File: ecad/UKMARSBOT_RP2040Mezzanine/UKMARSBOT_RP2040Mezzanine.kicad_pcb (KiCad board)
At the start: 2 copper layers, 99.1 x 81.3 mm, 20 parts, among them J3 Conn_01x06, J4 Conn_01x06, J5 Conn_01x03, J6 POWER, J7 Switch, M1 CONN_06SILK_FEMALE_PTH, M1 Left MOTOR, M2  CONN_06SILK_FEMALE_PTH, M2 Right MOTOR, U2 LM7805_TO220

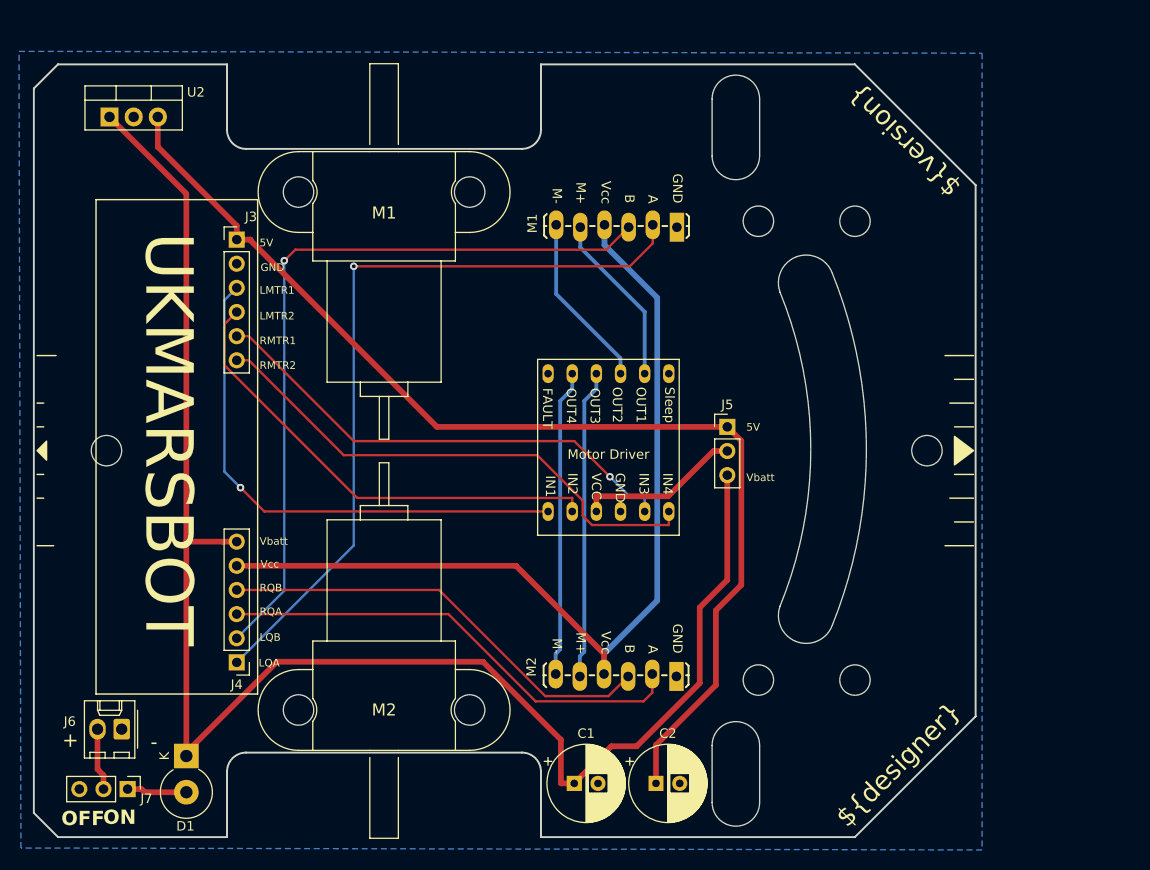
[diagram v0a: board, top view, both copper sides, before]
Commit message: fixed ignore file. Libraries from previous project. A verison of chassis, mezzanine and sensor board. Needed to play with connector locations. Nothing completly finished but i think the chassis and mezzanine are 90%
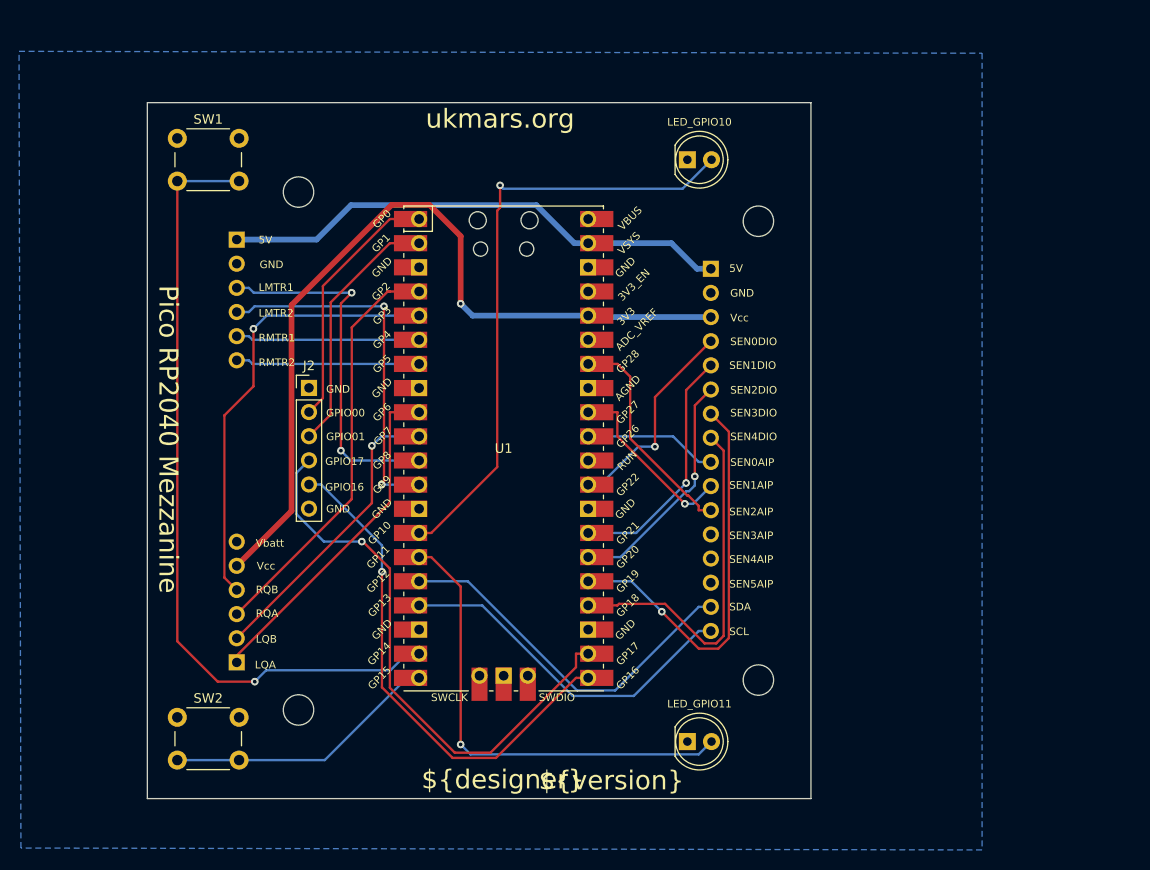
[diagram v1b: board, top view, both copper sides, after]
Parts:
- removed C1, C2: 330uF, 16V, Capacitor_THT:CP_Radial_D8.0mm_P2.50mm
- removed D1: 1N5401, Diode_THT:D_DO-201AE_P3.81mm_Vertical_KathodeUp
- removed H5, H6: MountingHole, ukmarsbot:MountingHole_3.2mm_M3_clearance
- removed J5: Conn_01x03, Connector_PinHeader_2.54mm:PinHeader_1x03_P2.54mm_Vertical
- removed J6: POWER, Connector_Molex:Molex_KK-254_AE-6410-02A_1x02_P2.54mm_Vertical
- removed J7: Switch, Connector_PinHeader_2.54mm:PinHeader_1x03_P2.54mm_Vertical
- removed M1: Left MOTOR, ukmarsbot:MINI-METAL-GEARMOTOR-WITH-BRACKET_Alt
- removed M1: CONN_06SILK_FEMALE_PTH, ukmarsbot:1X06_LOCK_LONGPADS
- removed M2: Right MOTOR, ukmarsbot:MINI-METAL-GEARMOTOR-WITH-BRACKET
- removed M2 : CONN_06SILK_FEMALE_PTH, ukmarsbot:1X06_LOCK_LONGPADS
- removed Motor Driver: DVR8833_DC_Controller, PBFootPrintLibrary:DRV8833_DC_Controller
- removed U2: LM7805_TO220, Package_TO_SOT_THT:TO-220-3_Vertical
- added J1: Conn_01x16, Connector_PinHeader_2.54mm:PinHeader_1x16_P2.54mm_Vertical, B.Cu at (139.4, 85.9)
- added J2: Conn_01x06, Connector_PinHeader_2.54mm:PinHeader_1x06_P2.54mm_Vertical, F.Cu at (97.1, 98.4)
- added LED_GPIO10: LED, LED_THT:LED_D5.0mm, F.Cu at (136.9, 74.4)
- added LED_GPIO11: LED, LED_THT:LED_D5.0mm, F.Cu at (136.9, 135.6)
- added SW1: TACT_SW, Button_Switch_THT:SW_PUSH_6mm, F.Cu at (83.2, 72.2)
- added SW2: TACT_SW, Button_Switch_THT:SW_PUSH_6mm, F.Cu at (83.2, 133.1)
- added U1: Pico, MCU_RaspberryPi_and_Boards:RPi_Pico_SMD_TH, F.Cu at (117.6, 104.8)
- J3, J4: moved to B.Cu
- moved H2 71.5 mm to (96.0, 132.3)
- moved H4 49.3 mm to (144.4, 129.1)
- moved H1 33.9 mm to (96.0, 77.8)
- turned J3 to 180 degrees
- turned J4 to 0 degrees
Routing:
- net Vbatt: track 169.6 -> 0.00 mm
- net GPIO14: track 0.00 -> 83.3 mm, vias 0 -> 1
- net GPIO10: track 0.00 -> 64.5 mm, vias 0 -> 1
- net 5V: track 118.0 -> 54.1 mm
- net GPIO17: track 0.00 -> 59.8 mm, vias 0 -> 1
- net GPIO16: track 0.00 -> 53.5 mm, vias 0 -> 1
- net GPIO11: track 0.00 -> 49.6 mm, vias 0 -> 1
- net LQB: track 79.5 -> 31.5 mm
- net LQA: track 81.2 -> 36.1 mm, vias 1 -> 0
- net SEN3DI0: track 0.00 -> 42.6 mm, vias 0 -> 1
- net SDA: track 0.00 -> 39.1 mm
- net SEN4DI0: track 0.00 -> 37.8 mm
- net SCL: track 0.00 -> 37.5 mm
- net RMTR2: track 55.0 -> 19.3 mm
- net RIGHT_MOTOR_1: track 32.6 -> 0.00 mm
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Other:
- board size 99.1 x 81.3 mm -> 69.8 x 73.2 mm
- board text added: "GPIO00"
- board text added: "GPIO01"
- board text added: "GPIO16"
- board text added: "GPIO17"
- board text added: "Pico RP2040 Mezzanine"
- board text added: "SCL"
- board text added: "SDA"
- board text added: "SEN0AIP"
- board text added: "SEN0DIO"
- board text added: "SEN1AIP"
- board text added: "SEN1DIO"
- board text added: "SEN2AIP"
- board text added: "SEN2DIO"
- board text added: "SEN3AIP"
- board text added: "SEN3DIO"
- board text added: "SEN4AIP"
- board text added: "SEN4DIO"
- board text added: "SEN5AIP"
- board text removed: "+"
- board text removed: "-"
- board text removed: "A"
- board text removed: "B"
- board text removed: "M+"
- board text removed: "M-"
- board text removed: "OFF"
- board text removed: "ON"
- board text removed: "PTO"
- board text removed: "UKMARSBOT"
- board text removed: "UKMARSBOT v2"

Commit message: Update to 5v rail and layouts across all 3 boards
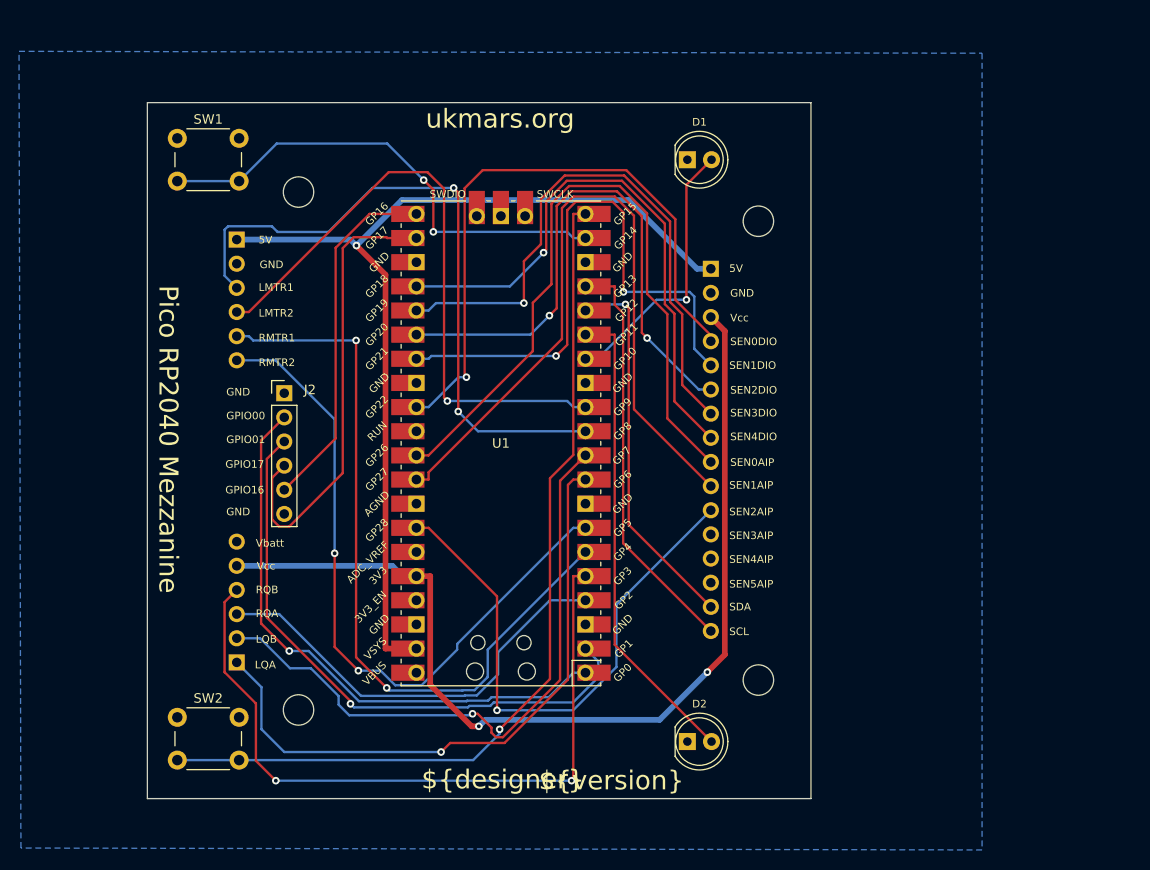
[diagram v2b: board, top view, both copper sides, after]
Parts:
- moved J2 2.66 mm to (94.5, 99.0)
- moved U1 0.61 mm to (117.3, 104.2), turned to 180 degrees
- renumbered LED_GPIO10 to D1, LED_GPIO11 to D2
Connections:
- U1 pad 42: GND -> unconnected-(U1-GND-Pad42)_1
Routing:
- net GPIO15: track 29.0 -> 94.2 mm, vias 0 -> 1
- net SEN0AIP: track 14.0 -> 74.1 mm
- net RMTR1: track 19.3 -> 79.4 mm, vias 0 -> 2
- net SEN1AIP: track 19.2 -> 76.3 mm, vias 1 -> 0
- net RMTR2: track 19.3 -> 72.1 mm, vias 0 -> 2
- net 5V: track 54.1 -> 102.0 mm, vias 0 -> 1
- net SEN0DI0: track 22.2 -> 66.0 mm
- net GPIO01: track 26.9 -> 63.1 mm, vias 0 -> 1
- net GPIO10: track 64.5 -> 29.0 mm
- net SEN1DI0: track 25.9 -> 61.3 mm, vias 1 -> 2
- net SEN2AIP: track 23.4 -> 58.5 mm, vias 0 -> 1
- net LQB: track 31.5 -> 66.5 mm
- net GPIO00: track 26.9 -> 61.4 mm, vias 0 -> 1
- net SEN2DI0: track 25.1 -> 59.3 mm, vias 1 -> 2
- net LMTR1: track 38.0 -> 71.0 mm
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
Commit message: Capacitor smoothing. Chassis placement changes, Mez board made smaller and added an additional LED
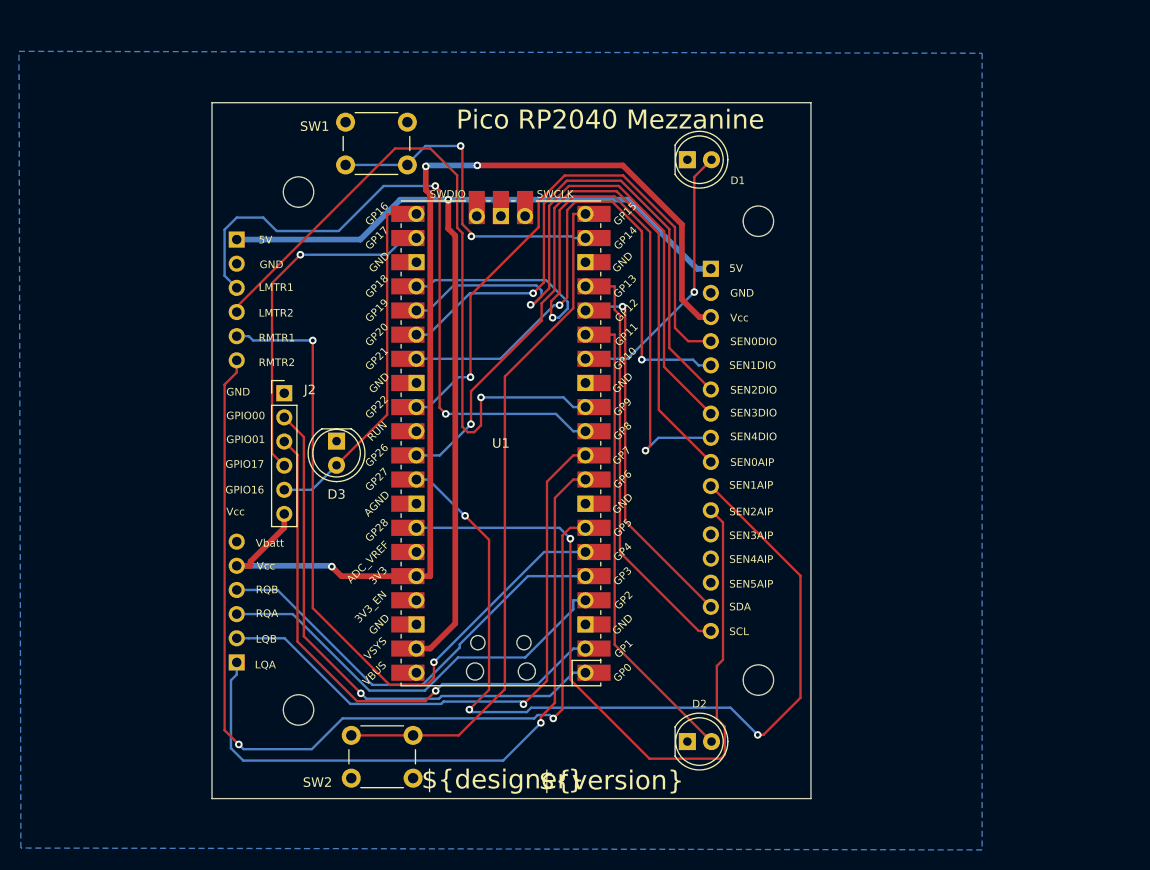
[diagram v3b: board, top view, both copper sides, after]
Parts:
- added D3: LED, LED_THT:LED_D5.0mm, F.Cu at (100.0, 104.0)
- moved SW2 25.6 mm to (108.0, 139.4), turned to 180 degrees
- moved SW1 17.8 mm to (101.0, 70.5)
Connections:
- J2 pad 6: GND -> Vcc
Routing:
- net RQB: track 76.8 -> 45.7 mm, vias 2 -> 0
- net RMTR2: track 72.1 -> 98.9 mm
- net GPIO15: track 94.2 -> 72.4 mm, vias 1 -> 0
- net SEN2AIP: track 58.5 -> 78.2 mm
- net SEN1AIP: track 76.3 -> 93.1 mm, vias 0 -> 3
- net GPIO14: track 51.3 -> 35.0 mm
- net SEN4DI0: track 60.1 -> 73.9 mm, vias 1 -> 2
- net GPIO17: track 48.2 -> 36.9 mm, vias 0 -> 1
- net Vcc: track 104.3 -> 113.7 mm, vias 2 -> 3
- net LMTR2: track 65.9 -> 75.3 mm
- net GPIO01: track 63.1 -> 56.8 mm
- net LQA: track 67.0 -> 72.3 mm
- net SEN0DI0: track 66.0 -> 61.1 mm
- net RMTR1: track 79.4 -> 75.1 mm
- net GPIO00: track 61.4 -> 57.3 mm
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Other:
- board size 69.8 x 73.2 mm -> 63 x 73.2 mm
- board text removed: "ukmars.org"

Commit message: Connectors moved to be on common 0.1" Grid and wheel cutouts included
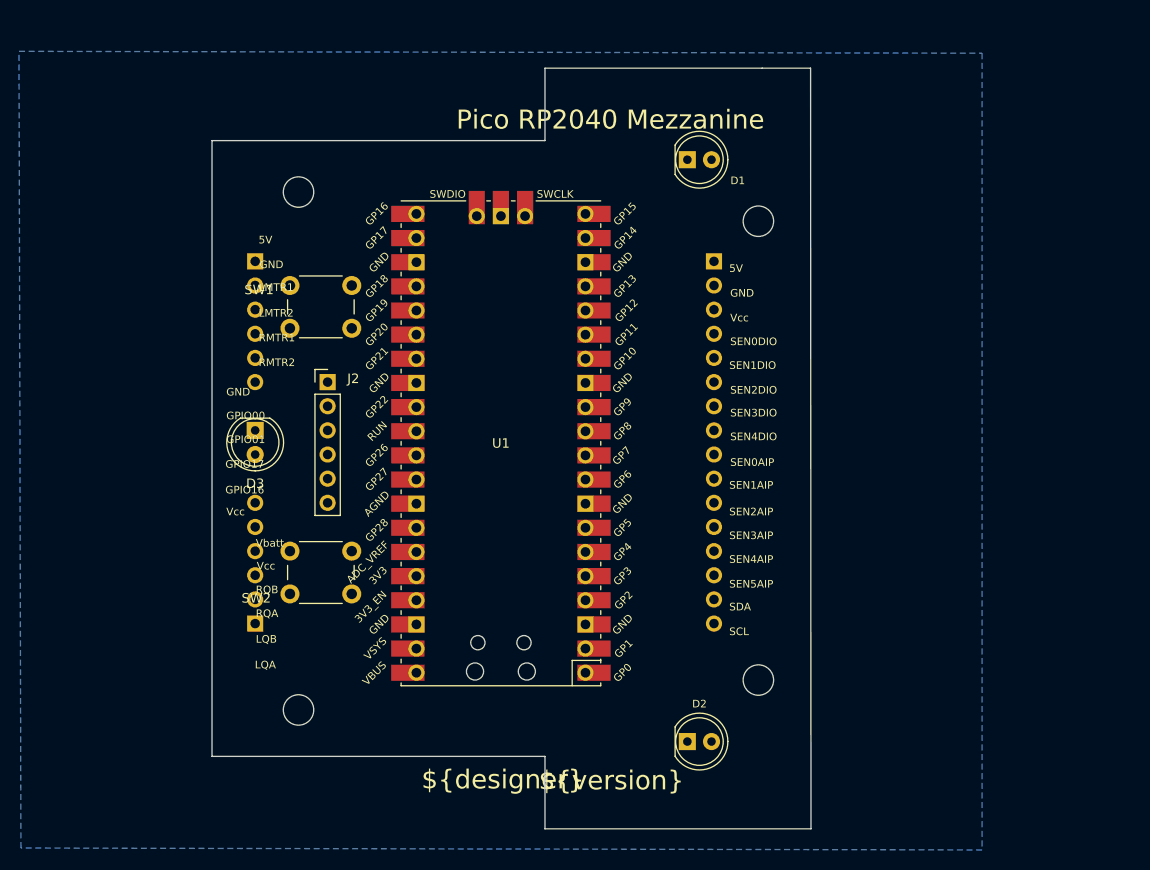
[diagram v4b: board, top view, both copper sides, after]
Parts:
- moved SW2 20.4 mm to (101.6, 120.1)
- moved SW1 18.1 mm to (95.1, 87.6)
- moved D3 8.63 mm to (91.4, 102.9)
- moved J2 4.71 mm to (99.1, 97.8)
- moved J4 4.52 mm to (91.4, 123.2)
- moved J3 3.00 mm to (91.4, 85.1)
- moved J1 0.85 mm to (139.7, 85.1)
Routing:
- net Vcc: track 113.7 -> 0.00 mm, vias 3 -> 0
- net 5V: track 104.7 -> 0.00 mm, vias 1 -> 0
- net RMTR2: track 98.9 -> 0.00 mm, vias 2 -> 0
- net SEN1AIP: track 93.1 -> 0.00 mm, vias 3 -> 0
- net SEN2AIP: track 78.2 -> 0.00 mm, vias 1 -> 0
- net LMTR2: track 75.3 -> 0.00 mm, vias 1 -> 0
- net RMTR1: track 75.1 -> 0.00 mm, vias 2 -> 0
- net SEN4DI0: track 73.9 -> 0.00 mm, vias 2 -> 0
- net SEN0AIP: track 73.3 -> 0.00 mm, vias 1 -> 0
- net GPIO15: track 72.4 -> 0.00 mm
- net LQA: track 72.3 -> 0.00 mm, vias 1 -> 0
- net LMTR1: track 71.8 -> 0.00 mm, vias 2 -> 0
- net SEN3DI0: track 64.1 -> 0.00 mm, vias 1 -> 0
- net LQB: track 62.9 -> 0.00 mm, vias 1 -> 0
- net SEN0DI0: track 61.1 -> 0.00 mm, vias 1 -> 0
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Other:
- board size 63 x 73.2 mm -> 63 x 80 mm

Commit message: Routed Chassis and Mezzanine Boards
Position and orientate motor connections to allow use of JST-SH breakout connectors.  Position and orientate spare pin breakout to accomodate bluetooth module. Re-assign pins and orientate Pico to facilitate routing.
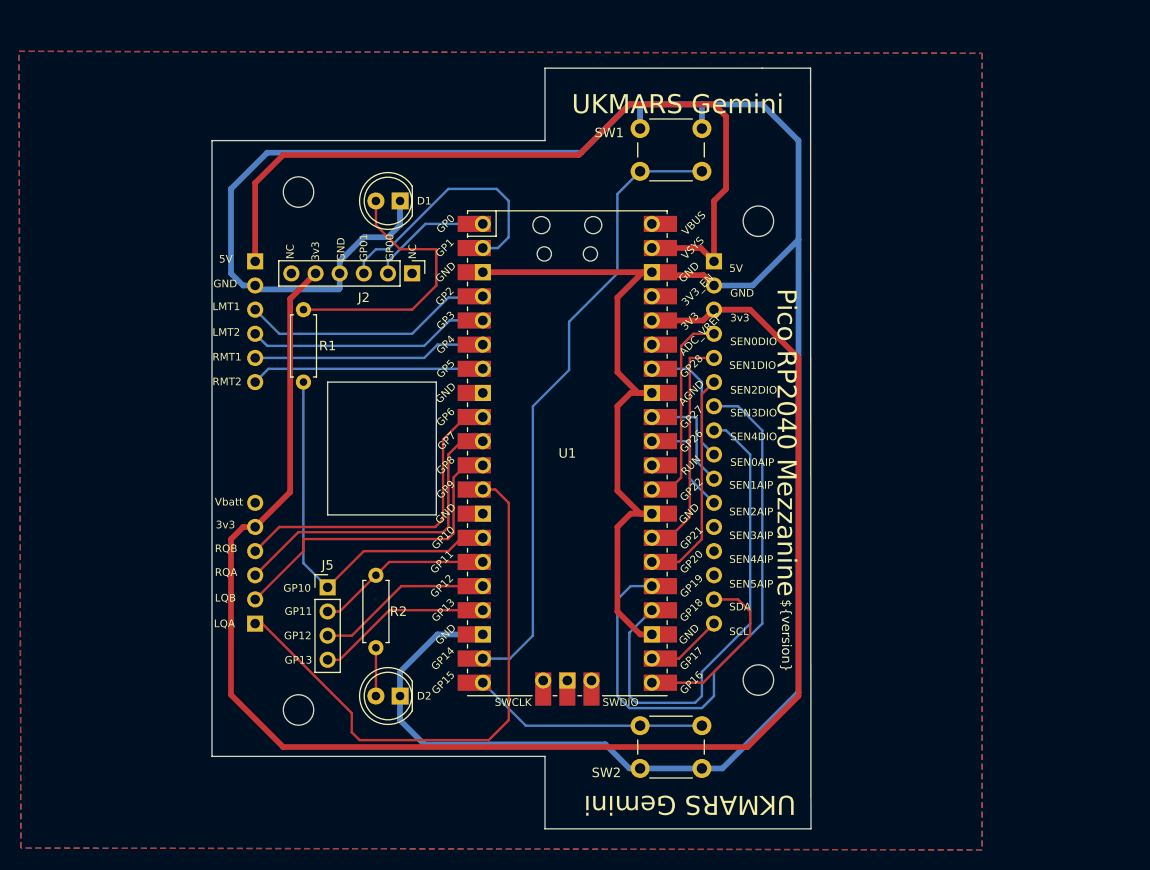
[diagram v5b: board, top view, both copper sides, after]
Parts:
- removed D3: LED, LED_THT:LED_D5.0mm
- added J5: Conn_01x04_Pin, Connector_PinHeader_2.54mm:PinHeader_1x04_P2.54mm_Vertical, F.Cu at (99.1, 119.4)
- added R1: 330R, Resistor_THT:R_Axial_DIN0207_L6.3mm_D2.5mm_P7.62mm_Horizontal, F.Cu at (96.5, 97.8)
- added R2: 330R, Resistor_THT:R_Axial_DIN0207_L6.3mm_D2.5mm_P7.62mm_Horizontal, F.Cu at (104.1, 118.1)
- moved SW2 41.2 mm to (138.4, 138.4)
- moved SW1 40.4 mm to (131.9, 71.1)
- moved D2 30.6 mm to (106.7, 130.8), turned to 180 degrees
- moved D1 30.5 mm to (106.7, 78.7), turned to 180 degrees
- moved J2 14.5 mm to (108.0, 86.4), turned to -90 degrees
- moved U1 7.06 mm to (124.3, 105.3), turned to 0 degrees
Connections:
- D1 pad 2: GPIO10 -> Net-(D1-A)
- D2 pad 2: GPIO11 -> Net-(D2-A)
- J1 pad 12: SEN3AIP -> unconnected-(J1-Pin_12-Pad12)
- J1 pad 13: SEN4AIP -> unconnected-(J1-Pin_13-Pad13)
- J1 pad 14: SEN5AIP -> unconnected-(J1-Pin_14-Pad14)
- J1 pad 3: Vcc -> 3v3
- J2 pad 1: GND -> unconnected-(J2-Pin_1-Pad1)
- J2 pad 4: GPIO17 -> GND
- J2 pad 5: GPIO16 -> 3v3
- J2 pad 6: Vcc -> unconnected-(J2-Pin_6-Pad6)
- J4 pad 5: Vcc -> 3v3
- U1 pad 10: LQB -> RQA
- U1 pad 11: LMTR1 -> LQB
- U1 pad 12: LMTR2 -> LQA
- U1 pad 16: SDA -> GPIO12
- U1 pad 17: SCL -> GPIO13
- U1 pad 21: GPIO16 -> SDA
- U1 pad 22: GPIO17 -> SCL
- U1 pad 31: SEN0AIP -> SEN2AIP
- U1 pad 34: SEN2AIP -> SEN0AIP
- U1 pad 36: Vcc -> 3v3
- U1 pad 4: RQA -> LMTR1
- U1 pad 5: RQB -> LMTR2
- U1 pad 9: LQA -> RQB
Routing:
- net GND: track 0.00 -> 313.6 mm
- net 3v3: track 0.00 -> 166.5 mm
- net 5V: track 0.00 -> 84.6 mm
- net GPIO14: track 0.00 -> 66.3 mm
- net SEN3DI0: track 0.00 -> 61.8 mm
- net LQA: track 0.00 -> 60.0 mm
- net SEN4DI0: track 0.00 -> 50.6 mm
- net GPIO10: track 0.00 -> 41.1 mm
- net LQB: track 0.00 -> 36.2 mm
- net RQB: track 0.00 -> 34.7 mm
- net RQA: track 0.00 -> 34.2 mm
- net Net-(D1-A): track 0.00 -> 28.8 mm
- net GPIO01: track 0.00 -> 27.2 mm
- net LMTR1: track 0.00 -> 26.6 mm
- net LMTR2: track 0.00 -> 25.6 mm
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- added copper zone on F.Cu, net GND
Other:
- outline, holes or cut-outs redrawn
- board text added: "3v3"
- board text added: "GP00"
- board text added: "GP01"
- board text added: "GP10"
- board text added: "GP11"
- board text added: "GP12"
- board text added: "GP13"
- board text added: "LMT1"
- board text added: "LMT2"
- board text added: "NC"
- board text added: "RMT1"
- board text added: "RMT2"
- board text added: "UKMARS Gemini"
- board text removed: "${designer}"
- board text removed: "GPIO00"
- board text removed: "GPIO01"
- board text removed: "GPIO16"
- board text removed: "GPIO17"
- board text removed: "LMTR1"
- board text removed: "LMTR2"
- board text removed: "RMTR1"
- board text removed: "RMTR2"
- board text removed: "Vcc"
